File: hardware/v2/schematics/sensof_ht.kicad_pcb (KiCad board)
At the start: 2 copper layers, 48 x 27 mm, 22 parts, among them U1 Si4010-GT, U2 HTU21D/Si7020

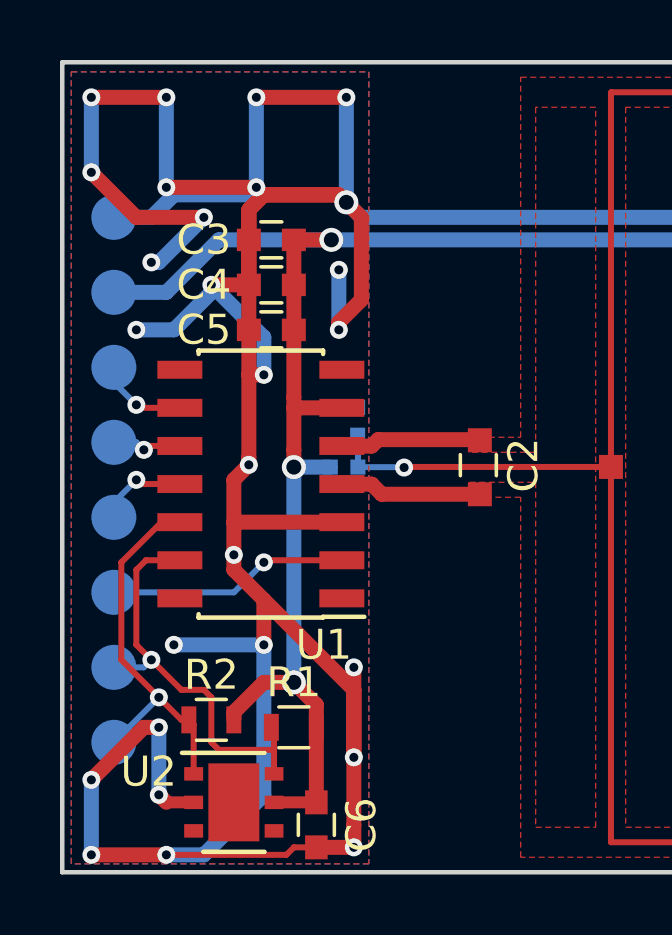
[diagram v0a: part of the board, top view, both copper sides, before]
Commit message: PCBv2: Updated Test pad possitions
Also removed a lot of ground traces that where there for the stitching
via's. But it seems KiCad 5 is smart enough to recognize via's in a fill
zone as belonging to that zone.
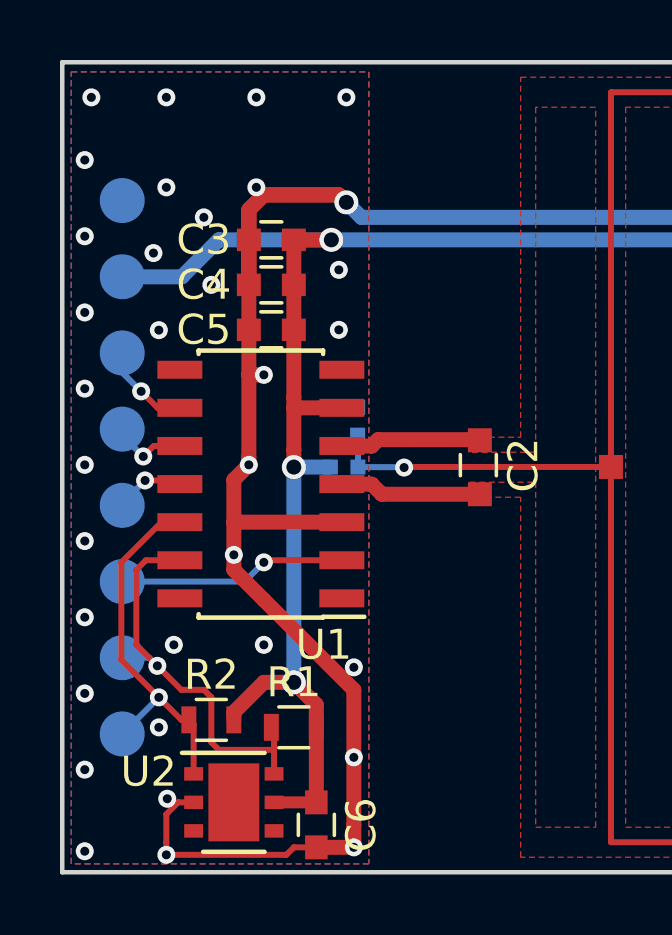
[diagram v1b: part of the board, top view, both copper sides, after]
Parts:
- moved TP8 0.63 mm to (126.0, 83.6)
- moved TP1 0.59 mm to (126.0, 86.1)
- moved TP7 0.56 mm to (126.0, 88.6)
- moved TP6 0.52 mm to (126.0, 91.2)
- moved TP5 0.49 mm to (126.0, 93.7)
- moved TP4 0.46 mm to (126.0, 96.3)
- moved TP3 0.43 mm to (126.0, 98.8)
- moved TP2 0.40 mm to (126.0, 101.3)
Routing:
- net GND: track 156.2 -> 77.2 mm, vias 28 -> 35
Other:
- board text added: "PN: 0003-00-01"
- board text removed: "PN: 0003-00-00"
